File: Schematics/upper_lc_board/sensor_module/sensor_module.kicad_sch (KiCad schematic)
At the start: 16 parts, among them J3 PT, J4 0.1uF

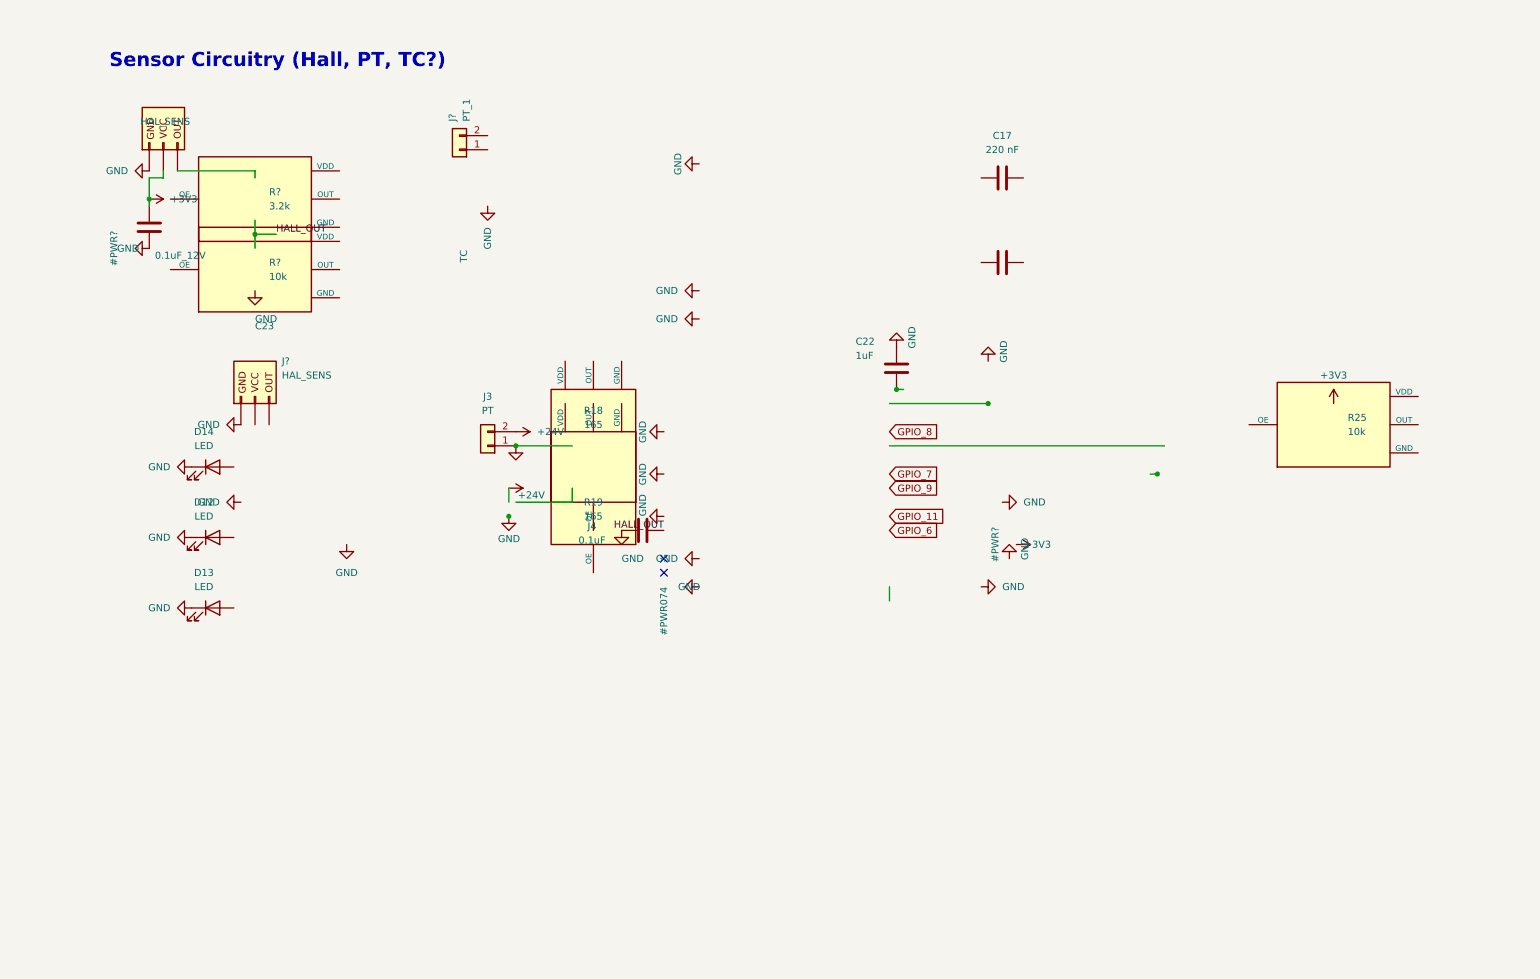
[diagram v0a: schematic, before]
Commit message: update layout with new connector
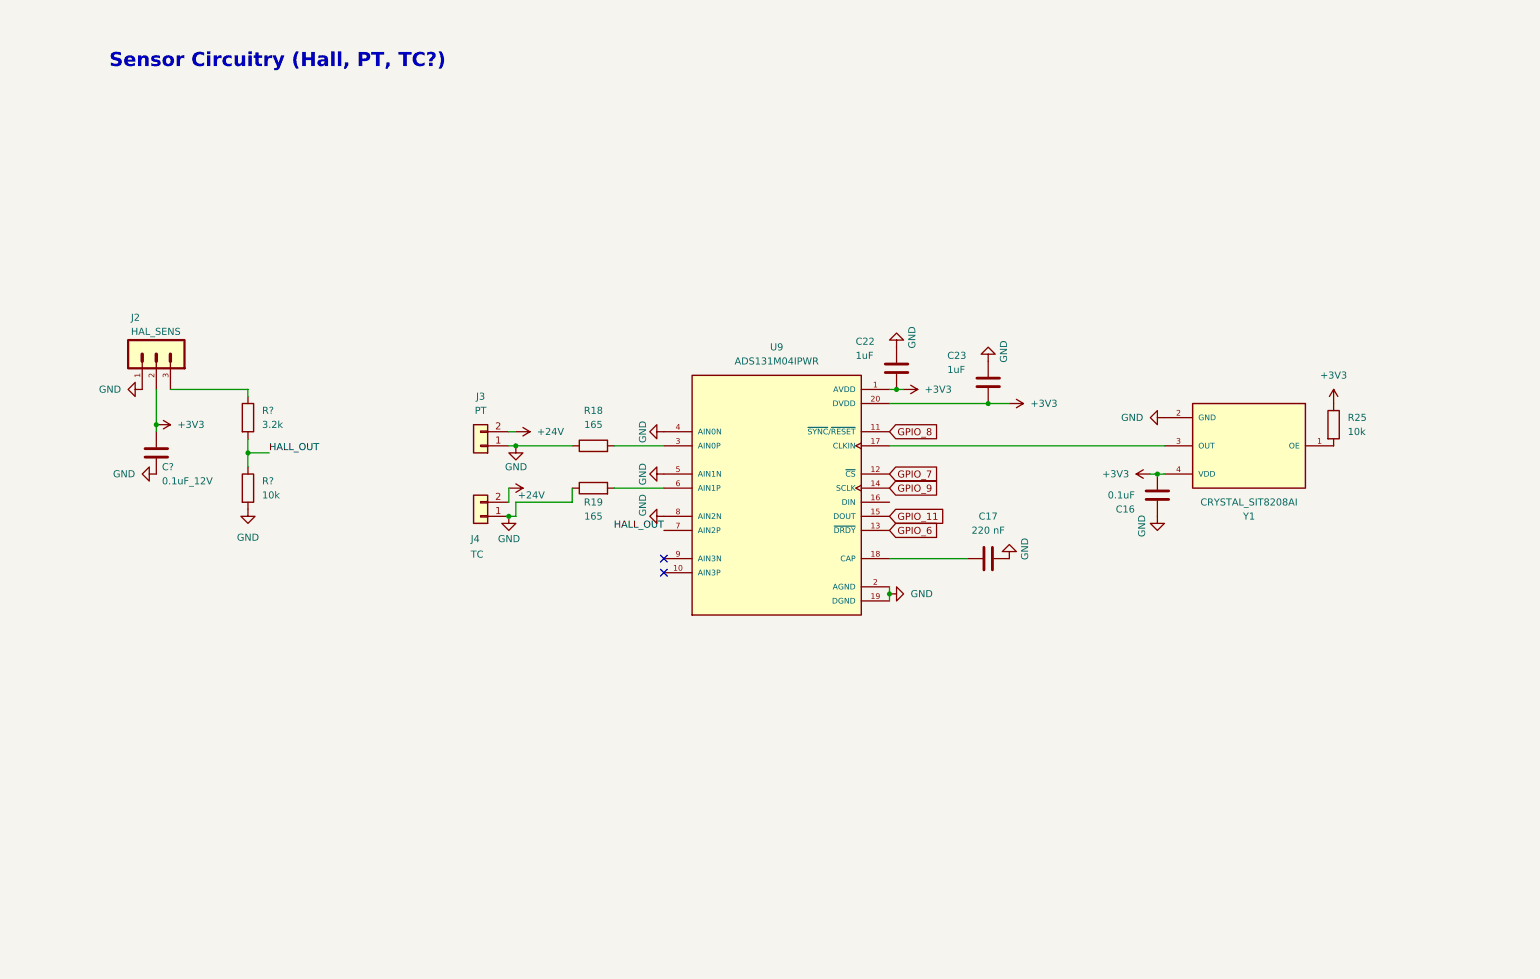
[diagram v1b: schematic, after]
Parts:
- removed D12, D13, D14: LED, symbol Device:LED
- removed J4: 0.1uF, Capacitor_SMD:C_0603_1608Metric, symbol Device:C
- removed J?: HAL_SENS, Connector_JST:JST_EH_S3B-EH_1x03_P2.50mm_Horizontal, symbol Connector_Generic:Conn_01x03
- removed J?: PT_1, Connector_JST:JST_EH_S2B-EH_1x02_P2.50mm_Horizontal, symbol Connector_Generic:Conn_01x02
- removed Y1: (no value), symbol Device:C
- added C16: 0.1uF, Capacitor_SMD:C_0603_1608Metric, symbol Device:C
- added C23: 1uF, Capacitor_SMD:C_0603_1608Metric, symbol Device:C
- added J2: HAL_SENS, 53048-0310:53048-0310, symbol 53048-0310:53048-0310
- added J4: TC, 530480210:MOLEX_530480210, symbol Connector_Generic:Conn_01x02
- added U9: ADS131M04IPWR, ADS131M04IPWR:SOP65P640X120-20N, symbol ADS131M04IPWR:ADS131M04IPWR
- added Y1: CRYSTAL_SIT8208AI, SIT8208AI-G3-33E-65.000000T:OSC_SIT8208AI-G3-33E-65.000000T, symbol SIT8208AI-G3-33E-65.000000T:SIT8208AI-G3-33E-65.000000T
- J3: footprint Connector_JST:JST_EH_S2B-EH_1x02_P2.50mm_Horizontal -> 530480210:MOLEX_530480210
- renumbered #PWR098 to C?
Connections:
- net TC is gone; now on net GND: J3.1 (Pin_1)
- net +24V: now also J4.2 (Pin_2)
- net +3V3: now also C22.2, R25.1, C16.2, C23.2, J2.2, U9.1 (AVDD), U9.20 (DVDD), Y1.4 (VDD)
- net GND: now also C17.2, R18.1, R19.1, R?.2, C16.1, C23.1, J2.1, J4.1 (Pin_1), U9.19 (DGND), U9.2 (AGND), U9.4 (AIN0N), U9.5 (AIN1N), U9.8 (AIN2N), Y1.2 (GND)
- net GPIO_11: now also U9.15 (DOUT)
- net GPIO_6: now also U9.13 (~{DRDY})
- net GPIO_7: now also U9.12 (~{CS})
- net GPIO_8: now also U9.11 (~{SYNC}/~{RESET})
- net GPIO_9: now also U9.14 (SCLK)
- net HALL_OUT: now also R?.1, R?.2, U9.7 (AIN2P)
- net at R25.2: now also Y1.1 (OE)
- net at R?.1: now also J2.3
- net at R19.2: now also U9.6 (AIN1P)
- net at R18.2: now also U9.3 (AIN0P)
- net at C17.1: now also U9.18 (CAP)
- new net: U9.17 (CLKIN), Y1.3 (OUT)
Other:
- moved on the sheet: J3

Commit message: 2nd temp commit for new ADC circuitry
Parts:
- added D14, D15, D16: LED, LED_SMD:LED_0805_2012Metric, symbol Device:LED
- added R28, R29, R30: 330, Capacitor_SMD:C_0402_1005Metric, symbol Device:R
- R25: footprint (none) -> Capacitor_SMD:C_0402_1005Metric
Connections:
- net GND: now also D14.1 (K), D15.1 (K), D16.1 (K)
- new net: D15.2 (A), R29.2
- new net: D14.2 (A), R28.2
- new net: D16.2 (A), R30.2
- new net GPIO_12: R30.1
- new net GPIO_13: R29.1
- new net GPIO_14: R28.1

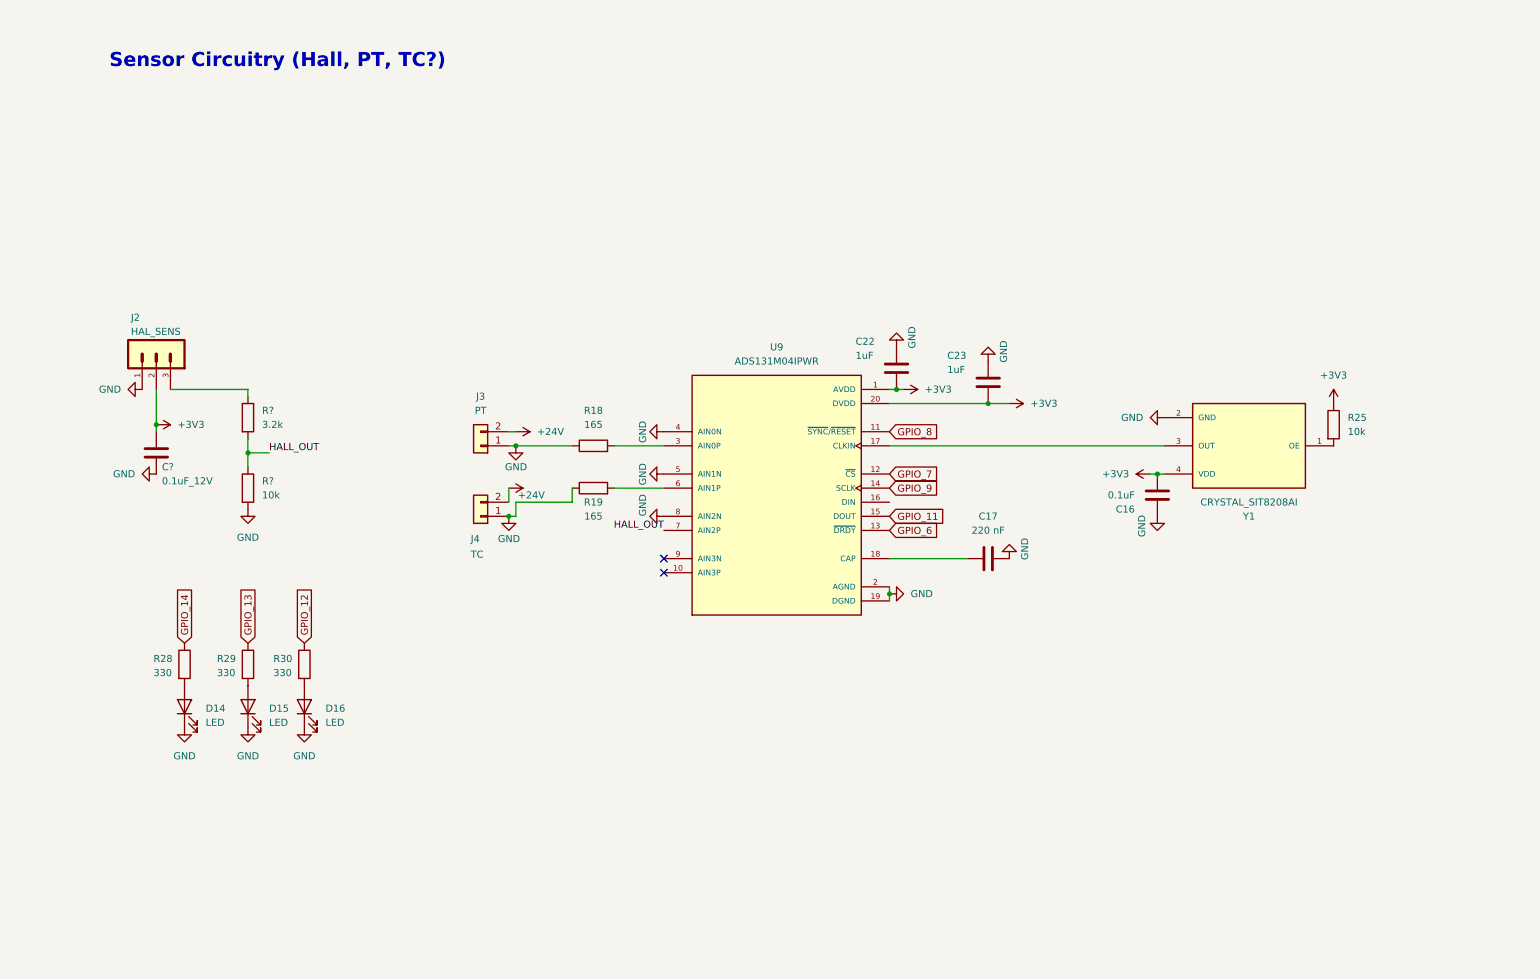
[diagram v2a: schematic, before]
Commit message: start redesigning ADC circuitry, organize schematic files. adding OPAMPS for buffered voltage divider on HALL & on PTs. layout to be adjusted after.
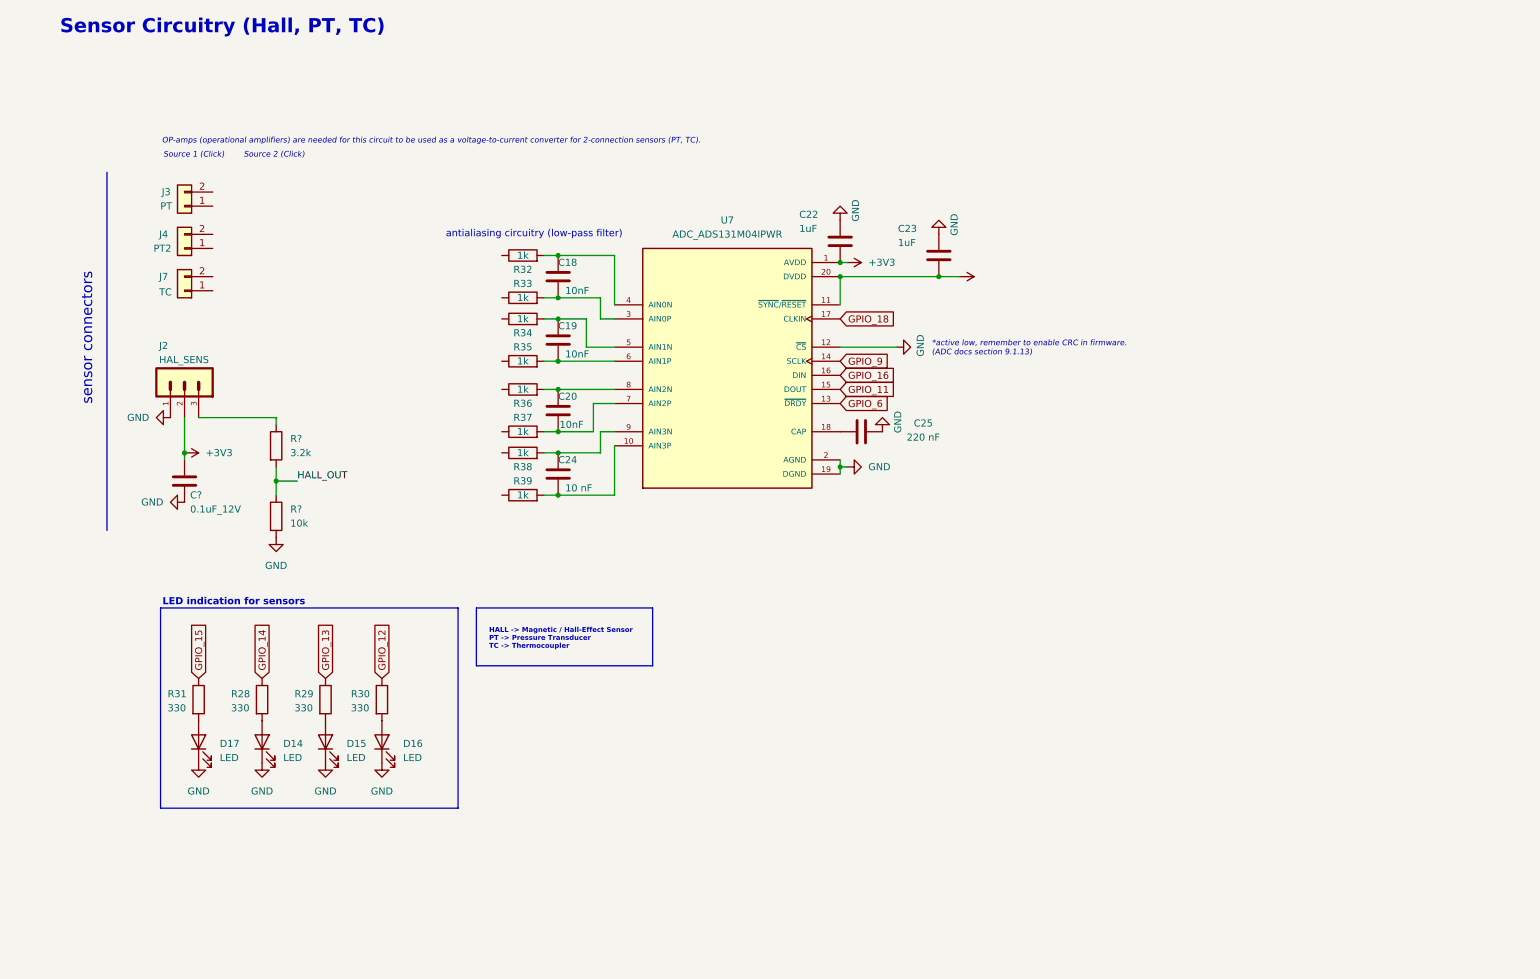
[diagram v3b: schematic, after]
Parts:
- removed C16: 0.1uF, Capacitor_SMD:C_0603_1608Metric, symbol Device:C
- removed C17: 220 nF, Capacitor_SMD:C_0402_1005Metric, symbol Device:C
- removed R18, R19: 165, Capacitor_SMD:C_0402_1005Metric, symbol Device:R
- removed R25: 10k, Capacitor_SMD:C_0402_1005Metric, symbol Device:R
- removed U9: ADS131M04IPWR, ADS131M04IPWR:SOP65P640X120-20N, symbol ADS131M04IPWR:ADS131M04IPWR
- removed Y1: CRYSTAL_SIT8208AI, SIT8208AI-G3-33E-65.000000T:OSC_SIT8208AI-G3-33E-65.000000T, symbol SIT8208AI-G3-33E-65.000000T:SIT8208AI-G3-33E-65.000000T
- added C18, C19, C20: 10nF, symbol Device:C
- added C24: 10 nF, symbol Device:C
- added C25: 220 nF, Capacitor_SMD:C_0402_1005Metric, symbol Device:C
- added D17: LED, LED_SMD:LED_0805_2012Metric, symbol Device:LED
- added J7: TC, 530480210:MOLEX_530480210, symbol Connector_Generic:Conn_01x02
- added R31: 330, Capacitor_SMD:C_0402_1005Metric, symbol Device:R
- added R32, R33, R34, R35, R36, R37, R38, R39: 1k, symbol Device:R
- added U7: ADC_ADS131M04IPWR, ADS131M04IPWR:SOP65P640X120-20N, symbol ADS131M04:ADS131M04IPWR
- J4: value TC -> PT2
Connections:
- net +3V3: now also U7.1 (AVDD), U7.11 (~{SYNC}/~{RESET}), U7.20 (DVDD)
- net GND: now also C25.2, D17.1 (K), U7.12 (~{CS}), U7.19 (DGND), U7.2 (AGND); no longer J3.1 (Pin_1), J4.1 (Pin_1)
- net GPIO_11: now also U7.15 (DOUT)
- net GPIO_6: now also U7.13 (~{DRDY})
- net GPIO_9: now also U7.14 (SCLK)
- net +24V: no longer names the net of J4.2 (Pin_2)
- net +24V: no longer J3.2 (Pin_2)
- new net: C20.2, R37.2, U7.7 (AIN2P)
- new net: C19.2, R35.2, U7.6 (AIN1P)
- new net: C20.1, R36.2, U7.8 (AIN2N)
- new net: C19.1, R34.2, U7.5 (AIN1N)
- new net: C24.2, R39.2, U7.10 (AIN3P)
- new net: C25.1, U7.18 (CAP)
- new net: C18.2, R33.2, U7.3 (AIN0P)
- new net: C18.1, R32.2, U7.4 (AIN0N)
- new net: C24.1, R38.2, U7.9 (AIN3N)
- new net: D17.2 (A), R31.2
- new net GPIO_15: R31.1
- new net GPIO_16: U7.16 (DIN)
- new net GPIO_18: U7.17 (CLKIN)
- no-connect marks 2 -> 0
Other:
- note added: "*active low, remember to enable CRC in firmware. (ADC docs section 9.1.13)"
- note added: "HALL -> Magnetic / Hall-Effect Sensor PT -> Pressure Transducer TC -> Thermocoupler"
- note added: "LED indication for sensors"
- note added: "OP-amps (operational amplifiers) are needed for this circuit to be used as a voltage-to-current converter for 2-connection sensors (PT, TC)."
- note added: "Sensor Circuitry (Hall, PT, TC)"
- note added: "Source 1 (Click)"
- note added: "Source 2 (Click)"
- note added: "antialiasing circuitry (low-pass filter)"
- note added: "sensor connectors"
- note removed: "Sensor Circuitry (Hall, PT, TC?)"
- moved on the sheet: C?, D14, D15, D16, J2, R28, R29, R30, R?

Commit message: start redesigning ADC circuitry, organize schematic files. adding OPAMPS for buffered voltage divider on HALL & on PTs. layout to be adjusted after.
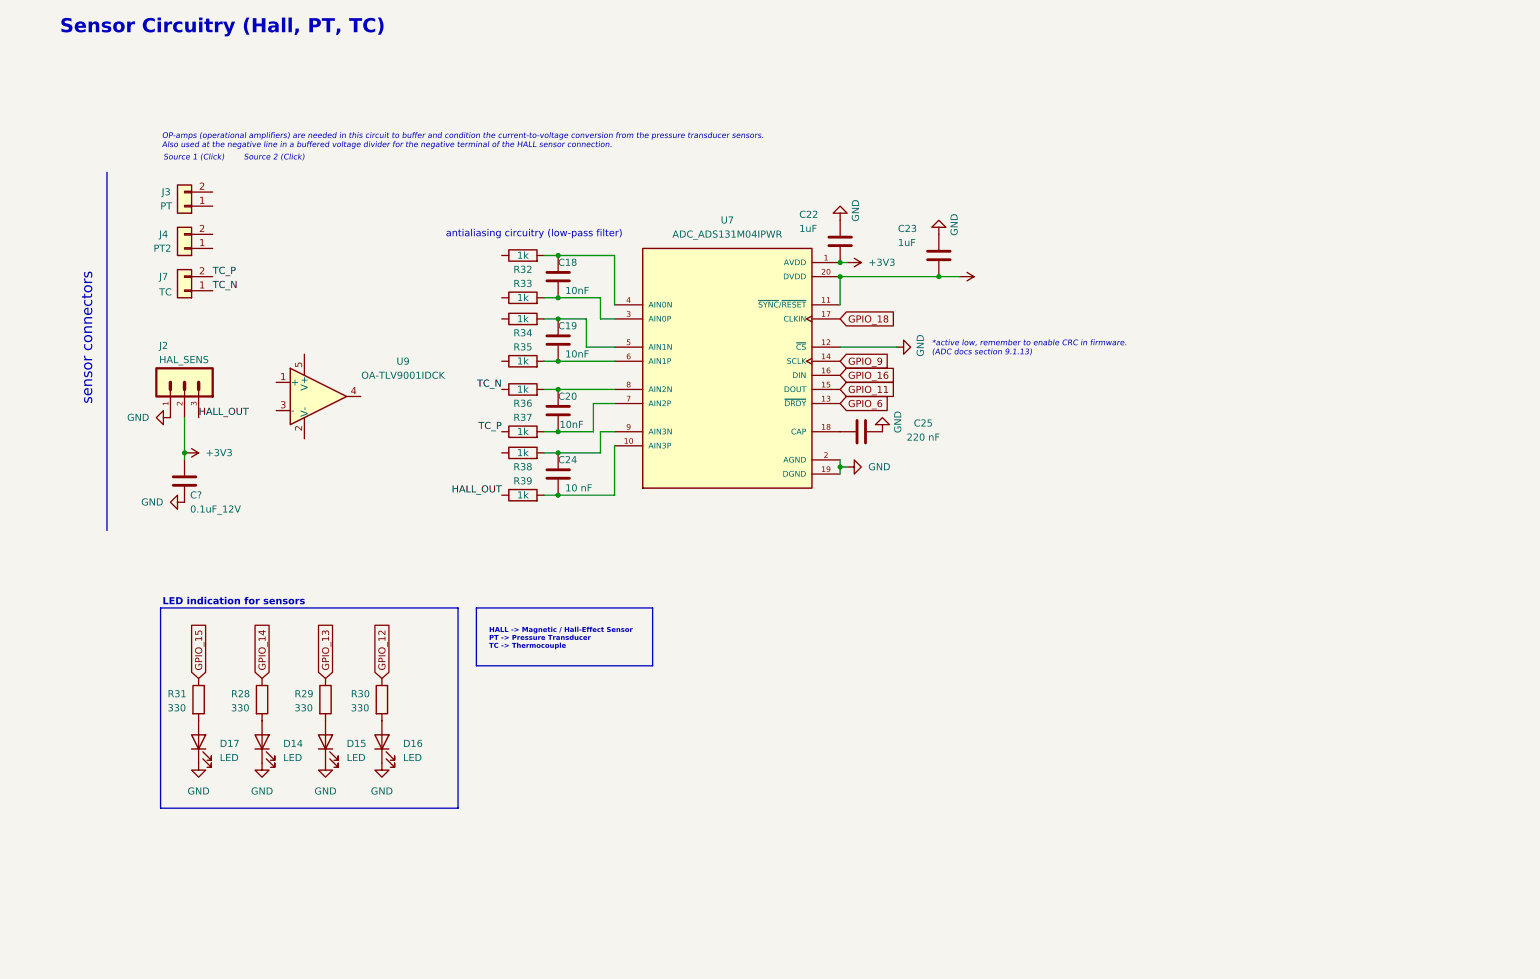
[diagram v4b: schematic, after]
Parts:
- removed R?: 10k, Capacitor_SMD:C_0402_1005Metric, symbol Device:R
- removed R?: 3.2k, Capacitor_SMD:C_0402_1005Metric, symbol Device:R
- added U9: OA-TLV9001IDCK, Package_TO_SOT_SMD:SOT-353_SC-70-5, symbol Amplifier_Operational:TLV9001IDCK
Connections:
- net HALL_OUT: now also J2.3, R39.1
- net TC_P: now reaches R37.1
- net TC_P: now also J7.2 (Pin_2)
- net TC_N: now reaches R36.1
- net TC_N: now also J7.1 (Pin_1)
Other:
- note added: "HALL -> Magnetic / Hall-Effect Sensor PT -> Pressure Transducer TC -> Thermocouple"
- note added: "OP-amps (operational amplifiers) are needed in this circuit to buffer and condition the current-to-voltage conversion from the pressure transducer sensors. Also used at the negative line in a buffered voltage divider for the negative terminal of the HALL sensor connection."
- note removed: "HALL -> Magnetic / Hall-Effect Sensor PT -> Pressure Transducer TC -> Thermocoupler"
- note removed: "OP-amps (operational amplifiers) are needed for this circuit to be used as a voltage-to-current converter for 2-connection sensors (PT, TC)."
